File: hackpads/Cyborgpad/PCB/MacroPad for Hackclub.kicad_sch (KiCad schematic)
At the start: 21 parts, among them SW1 SW_Push, SW10 RotaryEncoder, SW11 SW_Push, SW2 SW_Push, SW3 SW_Push, SW4 SW_Push, SW5 SW_Push, SW6 SW_Push, SW7 SW_Push, SW8 RotaryEncoder, SW9 SW_Push, U1 Seeed Studio XIAO SAMD21

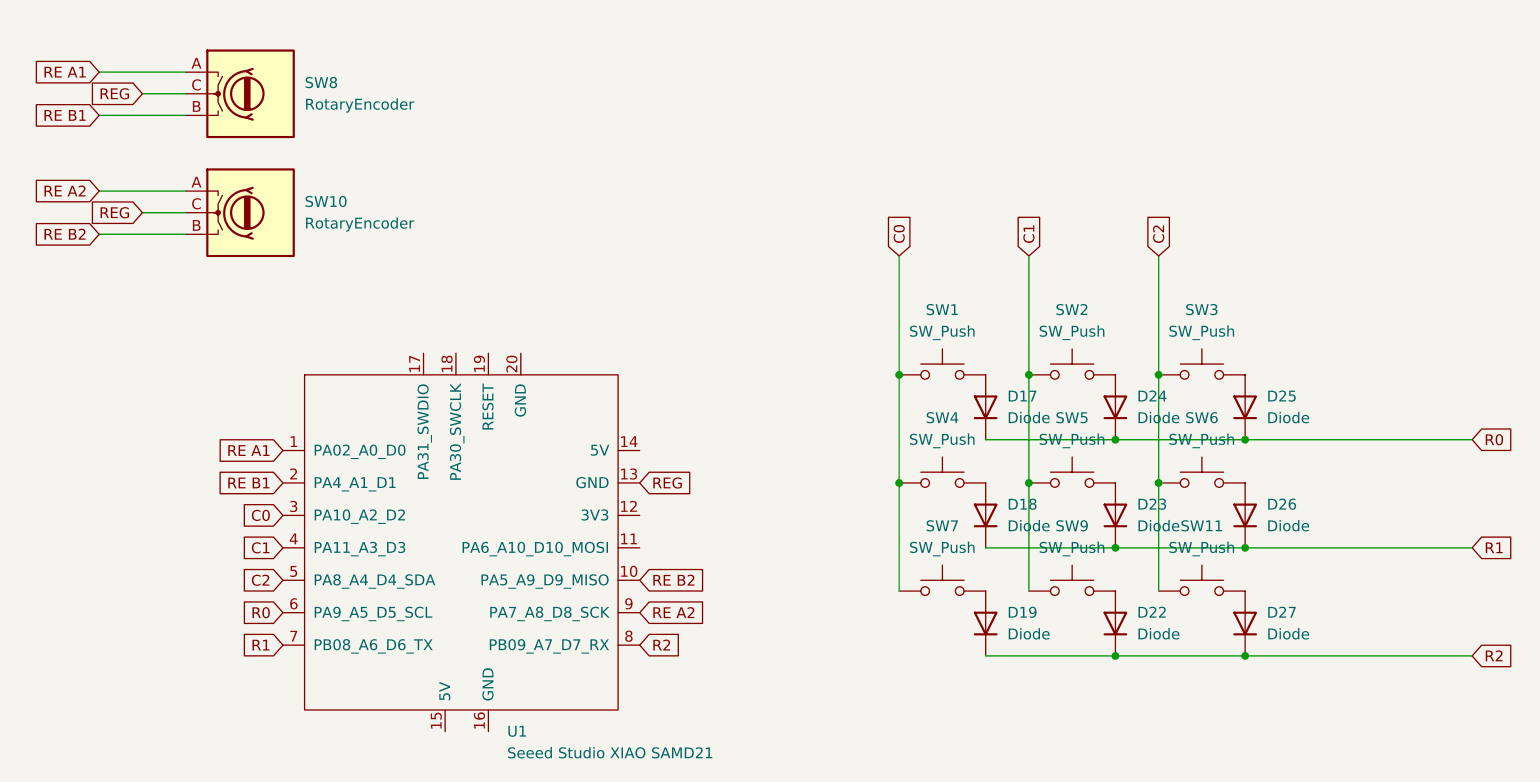
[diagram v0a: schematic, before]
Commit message: Add files via upload
Uploading Most Current PCB Files. Last ones uploaded were a previous version.
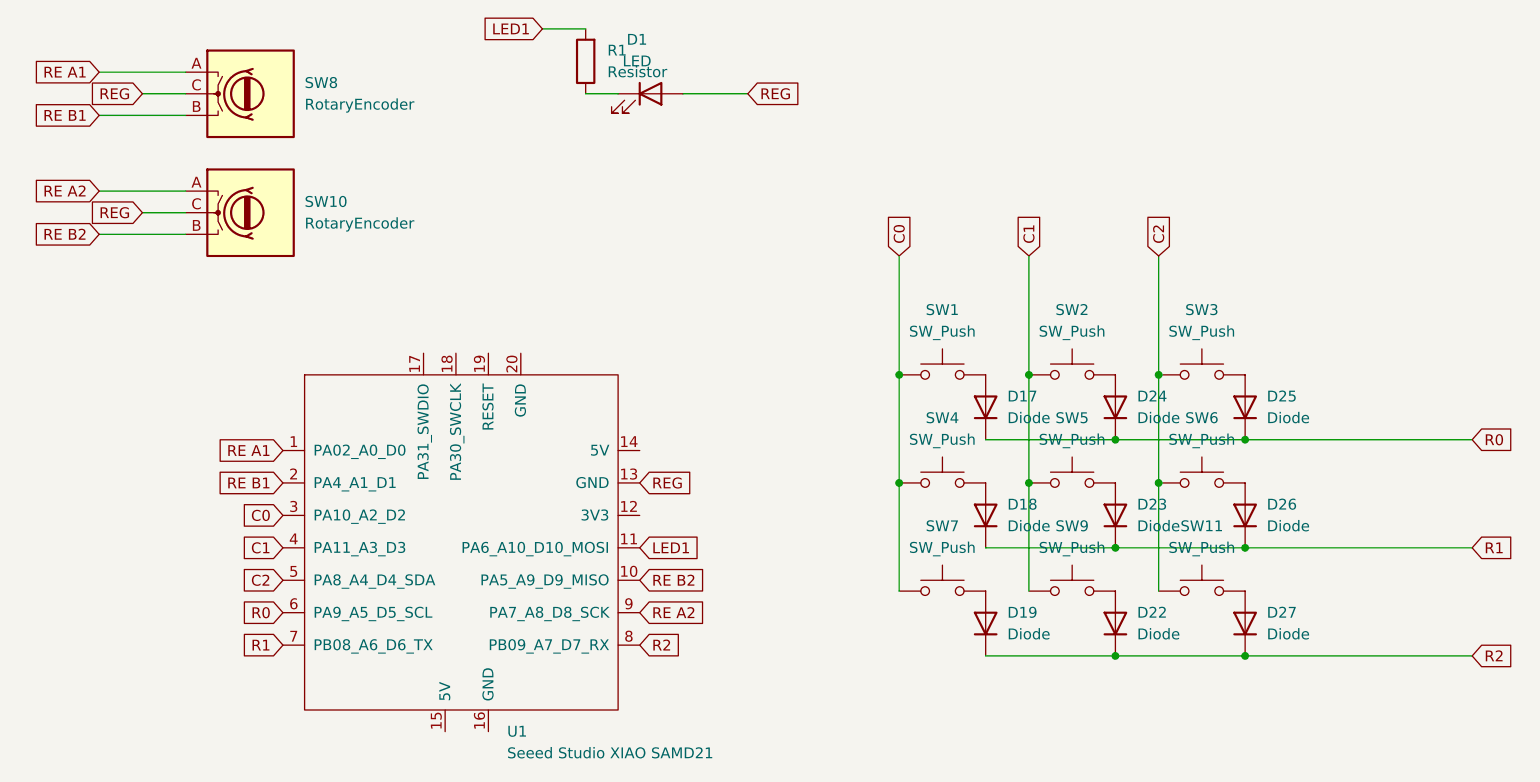
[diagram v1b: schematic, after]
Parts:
- added D1: LED, LED_THT:LED_D1.8mm_W1.8mm_H2.4mm_Horizontal_O1.27mm_Z8.2mm, symbol Device:LED
- added R1: Resistor, Resistor_THT:R_Axial_DIN0207_L6.3mm_D2.5mm_P7.62mm_Horizontal, symbol ScottoKeebs:Placeholder_Resistor
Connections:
- net REG: now also D1.2 (A)
- net LED1: now reaches U1.11 (PA6_A10_D10_MOSI)
- net LED1: now also R1.2
- new net: D1.1 (K), R1.1
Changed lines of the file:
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@@
+	(wire
+		(pts
+			(xy 95.25 41.91) (xy 100.33 41.91)
+		)
+		(stroke
+			(width 0)
+			(type default)
+		)
+	)
 	(wire
 		(pts
@@
 	(wire
 		(pts
+			(xy 119.38 49.53) (xy 111.76 49.53)
+		)
+		(stroke
+			(width 0)
+			(type default)
+		)
+	)
+	(wire
+		(pts
 			(xy 43.18 60.96) (xy 53.34 60.96)
 		)
@@
 	(wire
 		(pts
+			(xy 100.33 49.53) (xy 104.14 49.53)
+		)
+		(stroke
+			(width 0)
+			(type default)
+		)
+	)
+	(wire
+		(pts
 			(xy 152.4 95.25) (xy 152.4 107.95)
 		)
@@
 		)
 	)
+	(global_label "LED1"
+		(shape input)
+		(at 106.68 102.87 0)
+		(fields_autoplaced yes)
+		(effects
+			(font
+				(size 1.27 1.27)
+			)
+			(justify left)
+		)
+		(property "Intersheetrefs" "${INTERSHEET_REFS}"
+			(at 114.3218 102.87 0)
+			(effects
+				(font
+					(size 1.27 1.27)
+				)
+				(justify left)
+				(hide yes)
+			)
+		)
+	)
 	(global_label "RE B1"
 		(shape input)
@@
 		)
 	)
+	(global_label "LED1"
+		(shape input)
+		(at 95.25 41.91 180)
+		(fields_autoplaced yes)
+		(effects
+			(font
+				(size 1.27 1.27)
+			)
+			(justify right)
+		)
+		(property "Intersheetrefs" "${INTERSHEET_REFS}"
+			(at 87.6082 41.91 0)
+			(effects
+				(font
+					(size 1.27 1.27)
+				)
+				(justify right)
+				(hide yes)
+			)
+		)
+	)
 	(global_label "RE B2"
 		(shape input)
@@
 		)
 	)
+	(global_label "REG"
+		(shape input)
+		(at 119.38 49.53 0)
+		(fields_autoplaced yes)
+		(effects
+			(font
+				(size 1.27 1.27)
+			)
+			(justify left)
+		)
+		(property "Intersheetrefs" "${INTERSHEET_REFS}"
+			(at 126.0542 49.53 0)
+			(effects
+				(font
+					(size 1.27 1.27)
+				)
+				(justify left)
+				(hide yes)
+			)
+		)
+	)
 	(global_label "R0"
 		(shape input)
@@
 				(justify left)
 				(hide yes)
+			)
+		)
+	)
+	(symbol
+		(lib_id "ScottoKeebs:Placeholder_Resistor")
+		(at 100.33 45.72 90)
+		(unit 1)
+		(exclude_from_sim no)
+		(in_bom yes)
+		(on_board yes)
+		(dnp no)
+		(fields_autoplaced yes)
+		(property "Reference" "R1"
+			(at 102.87 44.4499 90)
+			(effects
+				(font
+					(size 1.27 1.27)
+				)
+				(justify right)
+			)
+		)
+		(property "Value" "Resistor"
+			(at 102.87 46.9899 90)
+			(effects
+				(font
+					(size 1.27 1.27)
+				)
+				(justify right)
+			)
+		)
+		(property "Footprint" "Resistor_THT:R_Axial_DIN0207_L6.3mm_D2.5mm_P7.62mm_Horizontal"
+			(at 102.108 45.72 0)
+			(effects
+				(font
+					(size 1.27 1.27)
+				)
+				(hide yes)
+			)
+		)
+		(property "Datasheet" "~"
+			(at 100.33 45.72 90)
+			(effects
+				(font
+					(size 1.27 1.27)
+				)
+				(hide yes)
+			)
+		)
+		(property "Description" "Resistor"
+			(at 100.33 45.72 0)
+			(effects
+				(font
+					(size 1.27 1.27)
+				)
+				(hide yes)
+			)
+		)
+		(pin "1"
+		)
+		(pin "2"
+		)
+		(instances
+			(project ""
+				(path "/99feb919-1c04-4a1a-9aa3-28ebe2478862"
+					(reference "R1")
+					(unit 1)
+				)
 			)
 		)
@@
 					(unit 1)
 				)
+			)
+		)
+	)
+	(symbol
+		(lib_id "Device:LED")
+		(at 107.95 49.53 0)
+		(unit 1)
+		(exclude_from_sim no)
+		(in_bom yes)
+		(on_board yes)
+		(dnp no)
+		(fields_autoplaced yes)
+		(property "Reference" "D1"
+			(at 106.3625 43.18 0)
+			(effects
+				(font
+					(size 1.27 1.27)
+				)
+			)
+		)
+		(property "Value" "LED"
+			(at 106.3625 45.72 0)
+			(effects
+				(font
+					(size 1.27 1.27)
+				)
+			)
+		)
+		(property "Footprint" "LED_THT:LED_D1.8mm_W1.8mm_H2.4mm_Horizontal_O1.27mm_Z8.2mm"
+			(at 107.95 49.53 0)
+			(effects
+				(font
+					(size 1.27 1.27)
+				)
+				(hide yes)
+			)
+		)
+		(property "Datasheet" "~"
+			(at 107.95 49.53 0)
+			(effects
+				(font
+					(size 1.27 1.27)
+				)
+				(hide yes)
+			)
+		)
+		(property "Description" "Light emitting diode"
+			(at 107.95 49.53 0)
+			(effects
+				(font
+					(size 1.27 1.27)
+				)
+				(hide yes)
+			)
+		)
+		(pin "1"
+		)
+		(pin "2"
+		)
+		(instances
+			(project ""
+				(path "/99feb919-1c04-4a1a-9aa3-28ebe2478862"
+					(reference "D1")
+					(unit 1)
+				)
